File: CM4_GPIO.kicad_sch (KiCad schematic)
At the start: 17 parts, among them J10 Conn_02x03_Odd_Even, J8 Conn_01x02, J9 THD-20-R, U6 74LVC1G07SE-7, U7 MagJack-A70-112-331N126

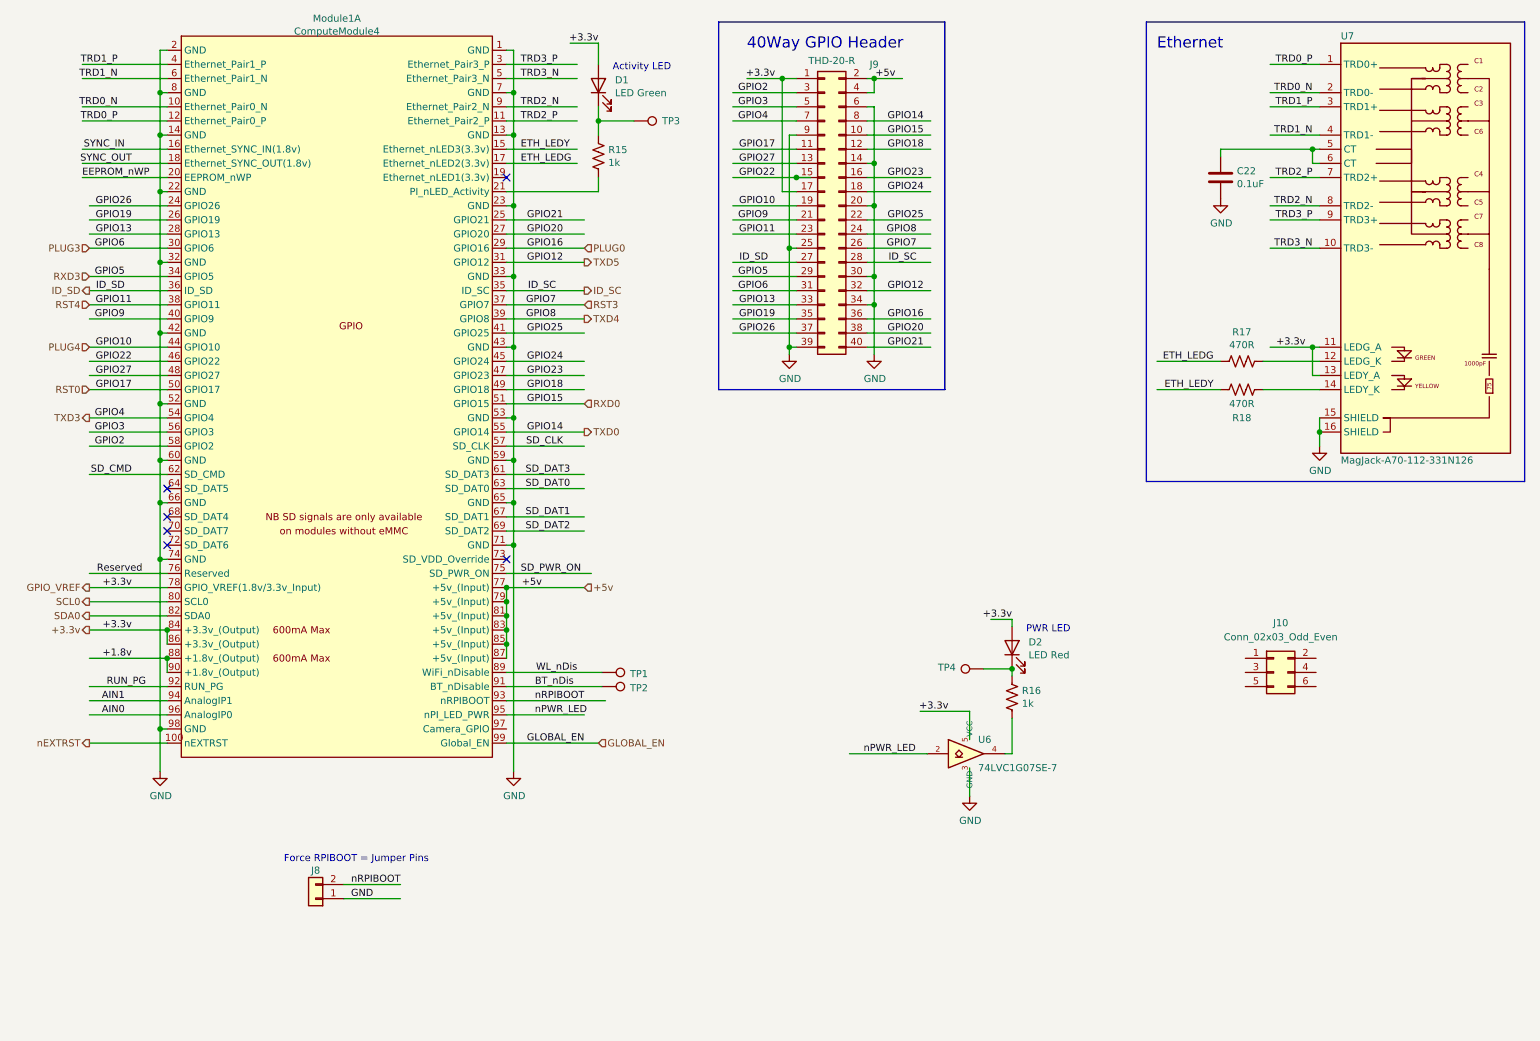
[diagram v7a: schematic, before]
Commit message: pulled in bitcrane fan and data connectors and edge cuts. most placement done. started routing
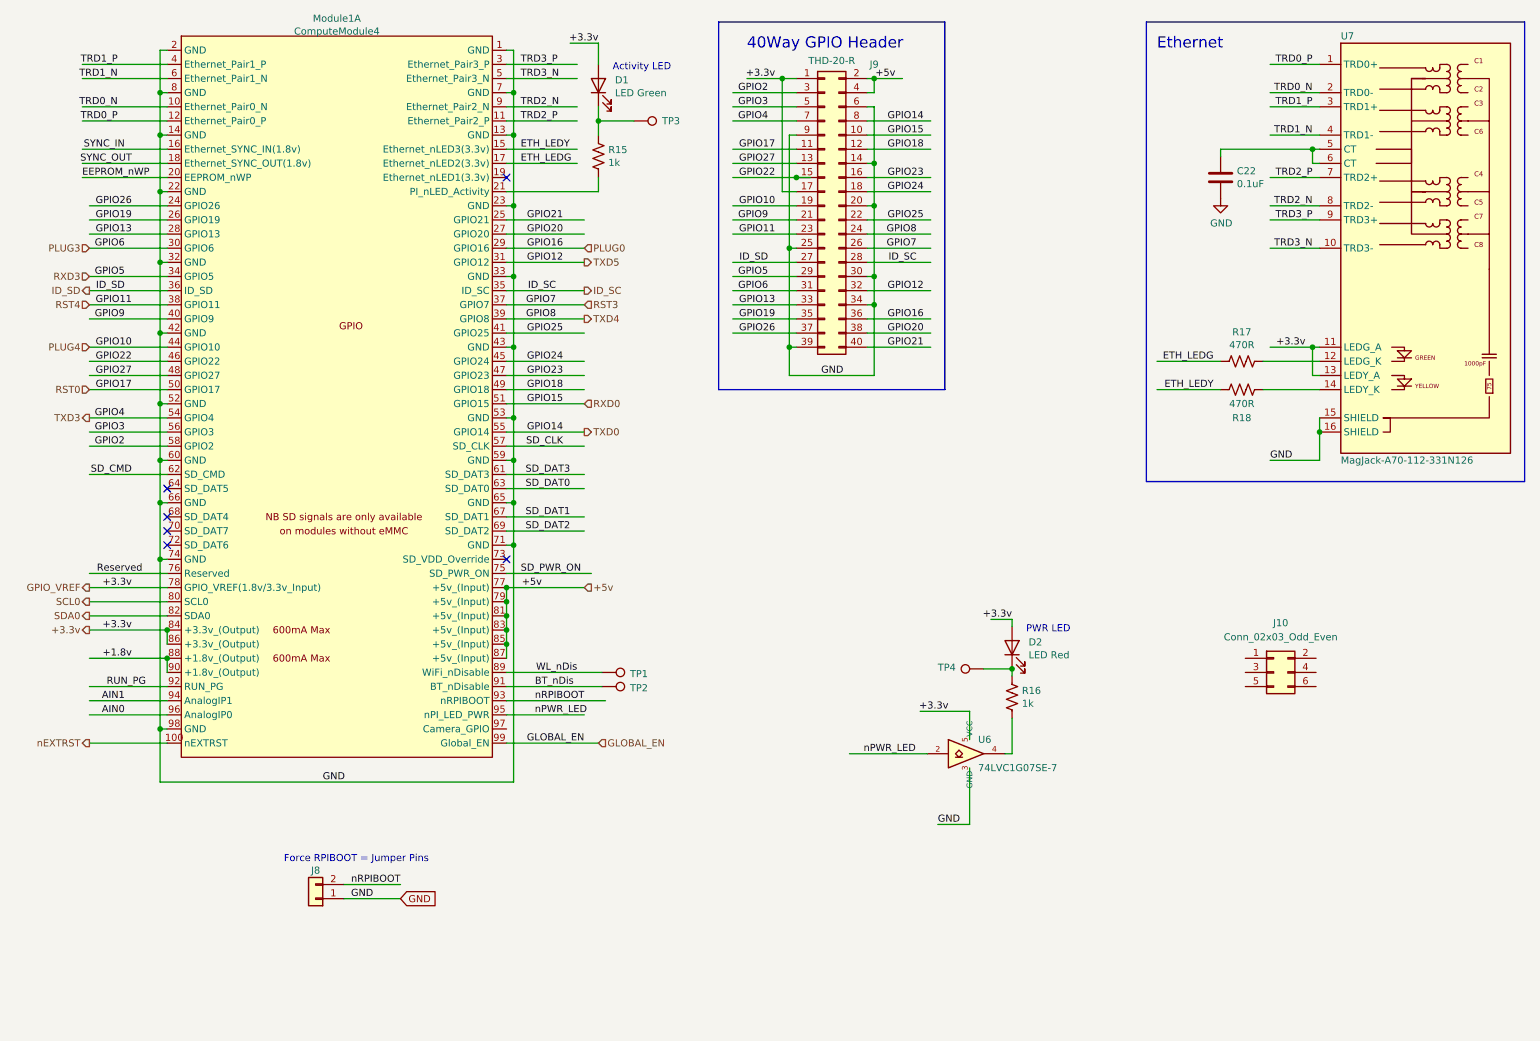
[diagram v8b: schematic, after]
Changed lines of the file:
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@@
   (title_block
     (title "Bitcart")
-    (date "2023-09-15")
+    (date "2024-02-26")
     (rev "1")
   )
@@
     (stroke (width 0) (type solid))
   )
+  (wire (pts (xy 177.8 158.115) (xy 183.515 158.115))
+    (stroke (width 0) (type solid))
+  )
   (wire (pts (xy 38.1 57.15) (xy 39.37 57.15))
     (stroke (width 0) (type solid))
   )
-  (wire (pts (xy 166.37 64.77) (xy 166.37 73.66))
+  (wire (pts (xy 166.37 64.77) (xy 166.37 77.47))
     (stroke (width 0) (type solid))
   )
@@
     (stroke (width 0) (type solid))
   )
-  (wire (pts (xy 101.6 107.95) (xy 101.6 148.59))
+  (wire (pts (xy 101.6 107.95) (xy 101.6 150.495))
     (stroke (width 0) (type solid))
   )
@@
   )
   (wire (pts (xy 100.33 52.07) (xy 114.3 52.07))
+    (stroke (width 0) (type solid))
+  )
+  (wire (pts (xy 38.1 150.495) (xy 101.6 150.495))
     (stroke (width 0) (type solid))
   )
@@
     (stroke (width 0) (type solid))
   )
-  (wire (pts (xy 183.515 147.955) (xy 183.515 153.035))
+  (wire (pts (xy 183.515 147.955) (xy 183.515 158.115))
     (stroke (width 0) (type solid))
   )
@@
     (stroke (width 0) (type solid))
   )
+  (wire (pts (xy 237.49 92.71) (xy 246.38 92.71))
+    (stroke (width 0) (type solid))
+  )
   (wire (pts (xy 165.1 34.29) (xy 176.53 34.29))
     (stroke (width 0) (type solid))
@@
   )
   (wire (pts (xy 25.4 64.77) (xy 39.37 64.77))
+    (stroke (width 0) (type solid))
+  )
+  (wire (pts (xy 166.37 77.47) (xy 151.13 77.47))
     (stroke (width 0) (type solid))
   )
@@
     (stroke (width 0) (type solid))
   )
-  (wire (pts (xy 246.38 87.63) (xy 246.38 90.17))
+  (wire (pts (xy 246.38 87.63) (xy 246.38 92.71))
     (stroke (width 0) (type solid))
   )
@@
     (stroke (width 0) (type solid))
   )
-  (wire (pts (xy 38.1 140.97) (xy 38.1 148.59))
+  (wire (pts (xy 38.1 140.97) (xy 38.1 150.495))
     (stroke (width 0) (type solid))
   )
@@
     (stroke (width 0) (type solid))
   )
-  (wire (pts (xy 151.13 72.39) (xy 151.13 73.66))
+  (wire (pts (xy 151.13 72.39) (xy 151.13 77.47))
     (stroke (width 0) (type solid))
   )
@@
     (effects (font (size 1.27 1.27)) (justify right bottom))
   )
+  (label "GND" (at 156.845 77.47 0) (fields_autoplaced)
+    (effects (font (size 1.27 1.27)) (justify left bottom))
+  )
   (label "GPIO3" (at 147.32 29.21 180) (fields_autoplaced)
     (effects (font (size 1.27 1.27)) (justify right bottom))
@@
   (label "GPIO18" (at 110.49 80.01 180) (fields_autoplaced)
     (effects (font (size 1.27 1.27)) (justify right bottom))
+  )
+  (label "GND" (at 177.8 158.115 0) (fields_autoplaced)
+    (effects (font (size 1.27 1.27)) (justify left bottom))
   )
   (label "GPIO15" (at 110.49 82.55 180) (fields_autoplaced)
@@
     (effects (font (size 1.27 1.27)) (justify right bottom))
   )
+  (label "GND" (at 67.31 150.495 0) (fields_autoplaced)
+    (effects (font (size 1.27 1.27)) (justify left bottom))
+  )
   (label "+3.3v" (at 33.02 123.19 180) (fields_autoplaced)
     (effects (font (size 1.27 1.27)) (justify right bottom))
@@
     (effects (font (size 1.27 1.27)) (justify right bottom))
   )
+  (label "GND" (at 237.49 92.71 0) (fields_autoplaced)
+    (effects (font (size 1.27 1.27)) (justify left bottom))
+  )
   (label "TRD0_N" (at 245.11 26.67 180) (fields_autoplaced)
     (effects (font (size 1.27 1.27)) (justify right bottom))
@@
   (label "AIN0" (at 31.75 138.43 180) (fields_autoplaced)
     (effects (font (size 1.27 1.27)) (justify right bottom))
+  )
+  (global_label "GND" (shape input) (at 81.28 171.45 0) (fields_autoplaced)
+    (effects (font (size 1.27 1.27)) (justify left))
+    (property "Intersheetrefs" "${INTERSHEET_REFS}" (at 88.2308 171.45 0)
+      (effects (font (size 1.27 1.27)) (justify left) hide)
+    )
   )
   (hierarchical_label "+5v" (shape input) (at 114.3 115.57 0) (fields_autoplaced)
@@
     )
   )
-  (symbol (lib_id "power:GND") (at 166.37 73.66 0) (unit 1)
-    (in_bom yes) (on_board yes) (dnp no)
-    (property "Reference" "#PWR033" (at 166.37 80.01 0)
-      (effects (font (size 1.27 1.27)) hide)
-    )
-    (property "Value" "GND" (at 166.497 78.0542 0)
-      (effects (font (size 1.27 1.27)))
-    )
-    (property "Footprint" "" (at 166.37 73.66 0)
-      (effects (font (size 1.27 1.27)) hide)
-    )
-    (property "Datasheet" "" (at 166.37 73.66 0)
-      (effects (font (size 1.27 1.27)) hide)
-    )
-    (pin "1")
-    (instances
-      (project "bitcart"
-        (path "/e63e39d7-6ac0-4ffd-8aa3-1841a4541b55/00000000-0000-0000-0000-00005cff706a"
-          (reference "#PWR033") (unit 1)
-        )
-      )
-    )
-  )
-  (symbol (lib_id "power:GND") (at 151.13 73.66 0) (unit 1)
-    (in_bom yes) (on_board yes) (dnp no)
-    (property "Reference" "#PWR032" (at 151.13 80.01 0)
-      (effects (font (size 1.27 1.27)) hide)
-    )
-    (property "Value" "GND" (at 151.257 78.0542 0)
-      (effects (font (size 1.27 1.27)))
-    )
-    (property "Footprint" "" (at 151.13 73.66 0)
-      (effects (font (size 1.27 1.27)) hide)
-    )
-    (property "Datasheet" "" (at 151.13 73.66 0)
-      (effects (font (size 1.27 1.27)) hide)
-    )
-    (pin "1")
-    (instances
-      (project "bitcart"
-        (path "/e63e39d7-6ac0-4ffd-8aa3-1841a4541b55/00000000-0000-0000-0000-00005cff706a"
-          (reference "#PWR032") (unit 1)
-        )
-      )
-    )
-  )
   (symbol (lib_id "Device:R_US") (at 232.41 74.93 270) (unit 1)
     (in_bom yes) (on_board yes) (dnp no)
@@
     )
   )
-  (symbol (lib_id "power:GND") (at 38.1 148.59 0) (unit 1)
-    (in_bom yes) (on_board yes) (dnp no)
-    (property "Reference" "#PWR030" (at 38.1 154.94 0)
-      (effects (font (size 1.27 1.27)) hide)
-    )
-    (property "Value" "GND" (at 38.227 152.9842 0)
-      (effects (font (size 1.27 1.27)))
-    )
-    (property "Footprint" "" (at 38.1 148.59 0)
-      (effects (font (size 1.27 1.27)) hide)
-    )
-    (property "Datasheet" "" (at 38.1 148.59 0)
-      (effects (font (size 1.27 1.27)) hide)
-    )
-    (pin "1")
-    (instances
-      (project "bitcart"
-        (path "/e63e39d7-6ac0-4ffd-8aa3-1841a4541b55/00000000-0000-0000-0000-00005cff706a"
-          (reference "#PWR030") (unit 1)
-        )
-      )
-    )
-  )
-  (symbol (lib_id "power:GND") (at 101.6 148.59 0) (unit 1)
-    (in_bom yes) (on_board yes) (dnp no)
-    (property "Reference" "#PWR031" (at 101.6 154.94 0)
-      (effects (font (size 1.27 1.27)) hide)
-    )
-    (property "Value" "GND" (at 101.727 152.9842 0)
-      (effects (font (size 1.27 1.27)))
-    )
-    (property "Footprint" "" (at 101.6 148.59 0)
-      (effects (font (size 1.27 1.27)) hide)
-    )
-    (property "Datasheet" "" (at 101.6 148.59 0)
-      (effects (font (size 1.27 1.27)) hide)
-    )
-    (pin "1")
-    (instances
-      (project "bitcart"
-        (path "/e63e39d7-6ac0-4ffd-8aa3-1841a4541b55/00000000-0000-0000-0000-00005cff706a"
-          (reference "#PWR031") (unit 1)
-        )
-      )
-    )
-  )
   (symbol (lib_id "Device:LED") (at 116.84 25.4 90) (unit 1)
     (in_bom yes) (on_board yes) (dnp no)
@@
     )
   )
-  (symbol (lib_id "power:GND") (at 183.515 153.035 0) (unit 1)
-    (in_bom yes) (on_board yes) (dnp no)
-    (property "Reference" "#PWR034" (at 183.515 159.385 0)
-      (effects (font (size 1.27 1.27)) hide)
-    )
-    (property "Value" "GND" (at 183.642 157.4292 0)
-      (effects (font (size 1.27 1.27)))
-    )
-    (property "Footprint" "" (at 183.515 153.035 0)
-      (effects (font (size 1.27 1.27)) hide)
-    )
-    (property "Datasheet" "" (at 183.515 153.035 0)
-      (effects (font (size 1.27 1.27)) hide)
-    )
-    (pin "1")
-    (instances
-      (project "bitcart"
-        (path "/e63e39d7-6ac0-4ffd-8aa3-1841a4541b55/00000000-0000-0000-0000-00005cff706a"
-          (reference "#PWR034") (unit 1)
-        )
-      )
-    )
-  )
   (symbol (lib_id "Device:LED") (at 191.135 126.365 90) (unit 1)
     (in_bom yes) (on_board yes) (dnp no)
@@
         )
       )
-    )
-  )
-  (symbol (lib_id "power:GND") (at 246.38 90.17 0) (unit 1)
-    (in_bom yes) (on_board yes) (dnp no)
-    (property "Reference" "#PWR036" (at 246.38 96.52 0)
-      (effects (font (size 1.27 1.27)) hide)
-    )
-    (property "Value" "GND" (at 246.507 94.5642 0)
-      (effects (font (size 1.27 1.27)))
-    )
-    (property "Footprint" "" (at 246.38 90.17 0)
-      (effects (font (size 1.27 1.27)) hide)
-    )
-    (property "Datasheet" "" (at 246.38 90.17 0)
-      (effects (font (size 1.27 1.27)) hide)
-    )
-    (pin "1")
-    (instances
-      (project "bitcart"
-        (path "/e63e39d7-6ac0-4ffd-8aa3-1841a4541b55/00000000-0000-0000-0000-00005cff706a"
-          (reference "#PWR036") (unit 1)
-        )
-      )
